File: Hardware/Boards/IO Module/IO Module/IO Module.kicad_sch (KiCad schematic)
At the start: 0 parts

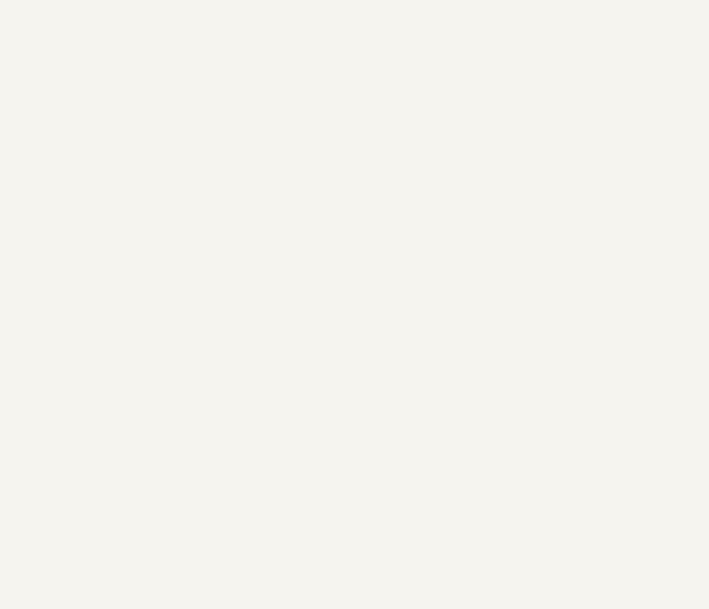
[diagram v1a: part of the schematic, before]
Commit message: Updated IO Module Schematics
Added MCU, JTAG and FIFO circuits
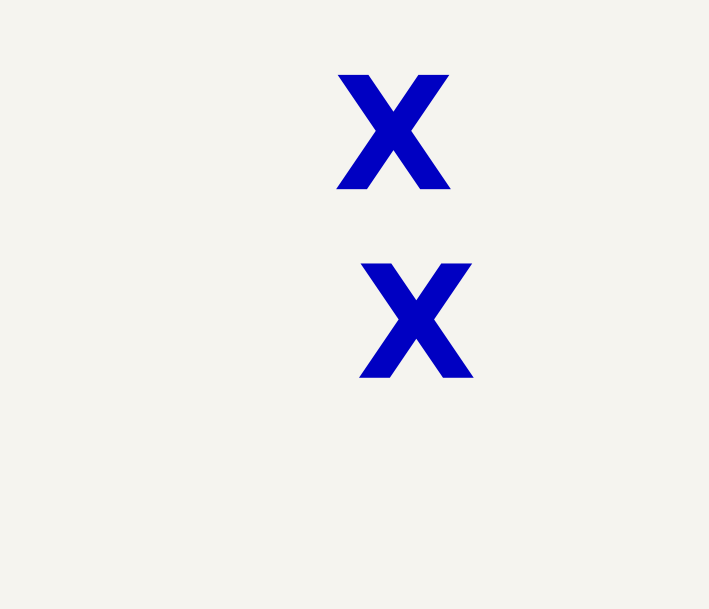
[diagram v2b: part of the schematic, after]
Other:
- note added: "X"
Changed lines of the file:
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@@
+		)
+	)
+	(text "X"
+		(exclude_from_sim no)
+		(at 259.08 159.385 0)
+		(effects
+			(font
+				(size 12.7 12.7)
+				(thickness 2.54)
+				(bold yes)
+				(color 255 0 34 1)
+			)
+		)
+	)
+	(text "X"
+		(exclude_from_sim no)
+		(at 261.62 180.34 0)
+		(effects
+			(font
+				(size 12.7 12.7)
+				(thickness 2.54)
+				(bold yes)
+				(color 255 0 34 1)
+			)
 		)
 	)
